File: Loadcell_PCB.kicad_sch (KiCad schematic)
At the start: 52 parts, among them J1 USB_C_Receptacle_USB2.0, J2 Load cell side, J3 Micro_SD_Card, Q1 S8550, SW1 RESET, U1 ATmega328P-M, U4 HX711, U5 74125, U6 LD1117S33TR_SOT223, U7 CH340C, Y1 16MHz

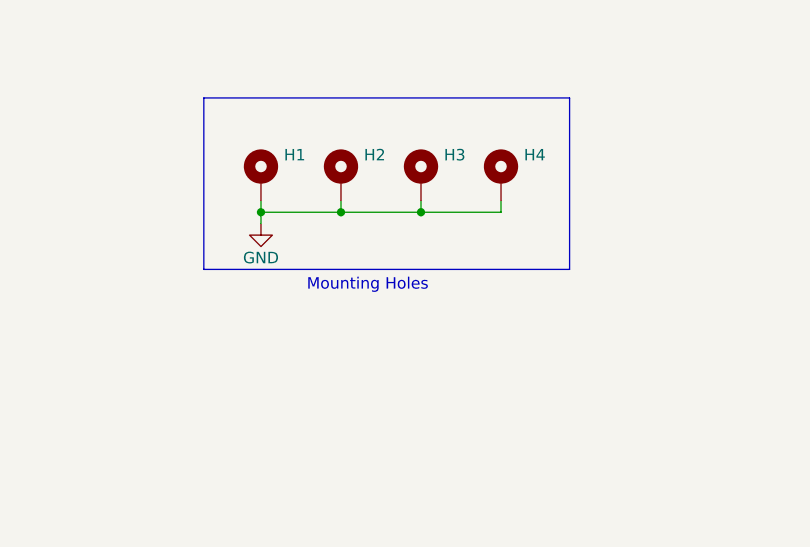
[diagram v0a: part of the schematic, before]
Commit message: some cleanup and add .gitignore
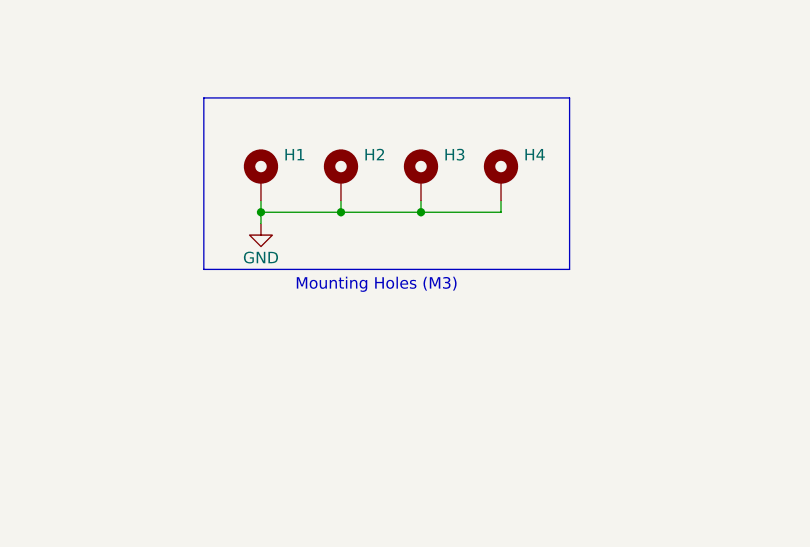
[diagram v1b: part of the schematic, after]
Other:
- note added: "Mounting Holes (M3)"
- note removed: "Mounting Holes"
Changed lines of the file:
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@@
     (effects (font (size 5 5)) (justify left bottom))
   )
-  (text "Mounting Holes\n" (at 203.2 242.57 0)
+  (text "Mounting Holes (M3)\n" (at 201.93 242.57 0)
     (effects (font (size 1.27 1.27)) (justify left bottom))
   )

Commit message: further cleanup for temp file
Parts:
- removed C4: 4u7F_16V, Capacitor_SMD:CP_Elec_4x3, symbol Device:C_Polarized
- removed D1: SS1P3L, Diode_SMD:D_Powermite_AK, symbol Device:D
- C6: renamed from C5; value 1uF -> 100nF
- renumbered C12 to C11, C13 to C12, C14 to C13, C15 to C14, C17 to C15, C9 to C2, C11 to C3, C3 to C4, C19 to C5, C6 to C7, C7 to C8, C18 to C9, D3 to D1, D6 to D3, D7 to D4, R17 to R1, R7 to R10, R9 to R11, R10 to R12, R12 to R13, R13 to R14, R14 to R15, R15 to R16, R16 to R2, R1 to R3, R2 to R4, R3 to R5, R4 to R6, R18 to R7, R19 to R8, R5 to R9, U7 to U2, U4 to U3, U5 to U4, U6 to U5
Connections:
- net VBUS is gone; now on net +5V: C2.1, C3.1, D1.1 (K)
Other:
- moved on the sheet: C4, C6

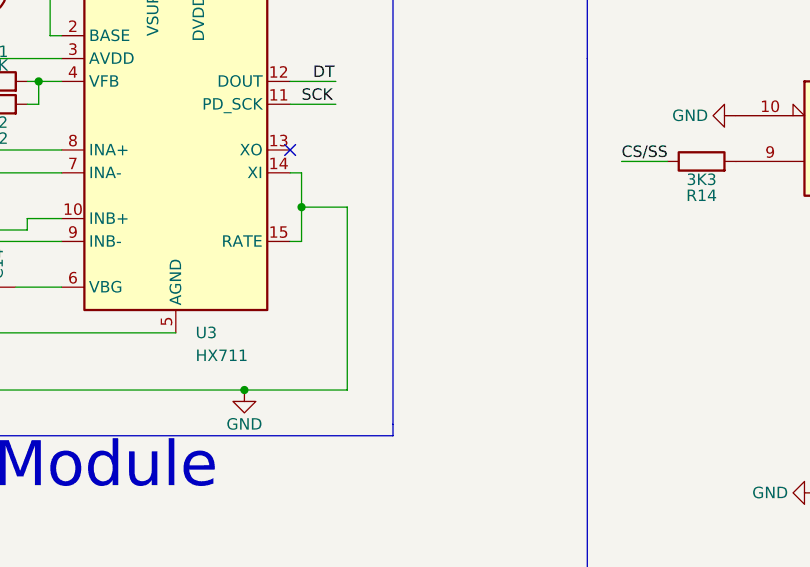
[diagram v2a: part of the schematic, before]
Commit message: Add pull-up resistor at rate pin on HX711 IC
Since HX711 can work in a higher frequency with rate pin pulled up, so I
add a optional structure that can select between two frequency by
soldering a ball at solder-jump bridge
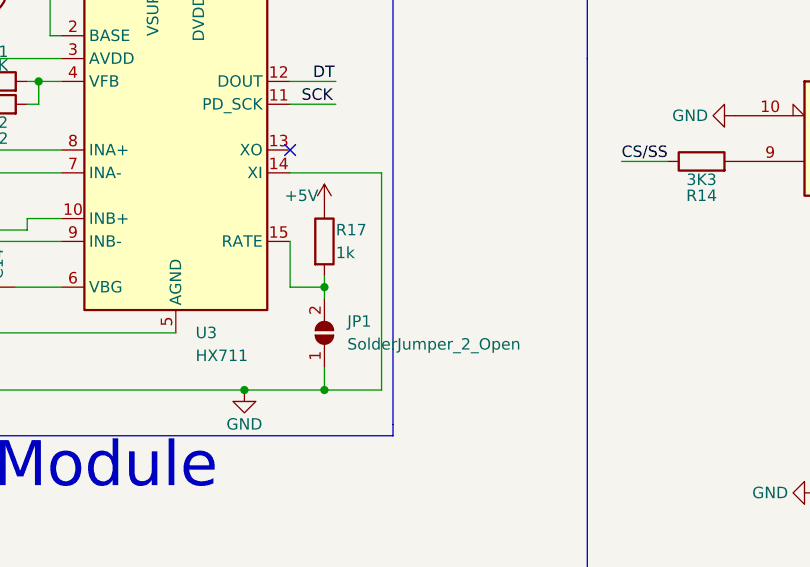
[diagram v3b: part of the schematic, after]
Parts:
- added JP1: SolderJumper_2_Open, Jumper:SolderJumper-2_P1.3mm_Open_RoundedPad1.0x1.5mm, symbol Jumper:SolderJumper_2_Open
- added R17: 1k, Resistor_SMD:R_0805_2012Metric_Pad1.20x1.40mm_HandSolder, symbol Device:R
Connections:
- net +5V: now also R17.1
- net GND: now also JP1.1 (A); no longer U3.15 (RATE)
- new net: JP1.2 (B), R17.2, U3.15 (RATE)
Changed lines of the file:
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@@
   (title_block
     (title "Loadcell_PCB")
-    (date "2024-02-08")
-    (rev "1.3")
+    (date "2024-03-06")
+    (rev "1.5")
     (company "NCKU_ISP")
     (comment 1 "https://hackmd.io/@ispncku/BywRPedI6")
@@
   (junction (at 198.12 233.68) (diameter 0) (color 0 0 0 0)
   )
-  (junction (at 260.35 152.4) (diameter 0) (color 0 0 0 0)
-  )
   (junction (at 69.85 154.94) (diameter 0) (color 0 0 0 0)
   )
@@
   (junction (at 243.84 120.65) (diameter 0) (color 0 0 0 0)
   )
+  (junction (at 262.89 161.29) (diameter 0) (color 0 0 0 0)
+  )
   (junction (at 218.44 144.78) (diameter 0) (color 0 0 0 0)
+  )
+  (junction (at 262.89 172.72) (diameter 0) (color 0 0 0 0)
   )
   (junction (at 54.61 167.64) (diameter 0) (color 0 0 0 0)
@@
     (stroke (width 0) (type default))
   )
+  (wire (pts (xy 259.08 156.21) (xy 259.08 161.29))
+    (stroke (width 0) (type default))
+  )
   (wire (pts (xy 198.12 156.21) (xy 198.12 148.59))
     (stroke (width 0) (type default))
@@
     (stroke (width 0) (type default))
   )
-  (wire (pts (xy 260.35 152.4) (xy 260.35 156.21))
+  (wire (pts (xy 259.08 161.29) (xy 262.89 161.29))
+    (stroke (width 0) (type default))
+  )
+  (wire (pts (xy 262.89 160.02) (xy 262.89 161.29))
     (stroke (width 0) (type default))
   )
@@
     (stroke (width 0) (type default))
   )
+  (wire (pts (xy 259.08 148.59) (xy 269.24 148.59))
+    (stroke (width 0) (type default))
+  )
   (wire (pts (xy 95.25 87.63) (xy 95.25 88.9))
     (stroke (width 0) (type default))
@@
     (stroke (width 0) (type default))
   )
-  (wire (pts (xy 265.43 172.72) (xy 265.43 152.4))
+  (wire (pts (xy 269.24 148.59) (xy 269.24 172.72))
     (stroke (width 0) (type default))
   )
@@
     (stroke (width 0) (type default))
   )
+  (wire (pts (xy 254 172.72) (xy 262.89 172.72))
+    (stroke (width 0) (type default))
+  )
+  (wire (pts (xy 262.89 161.29) (xy 262.89 162.56))
+    (stroke (width 0) (type default))
+  )
   (wire (pts (xy 53.34 167.64) (xy 54.61 167.64))
     (stroke (width 0) (type default))
@@
     (stroke (width 0) (type default))
   )
+  (wire (pts (xy 262.89 172.72) (xy 269.24 172.72))
+    (stroke (width 0) (type default))
+  )
   (wire (pts (xy 218.44 161.29) (xy 220.98 161.29))
     (stroke (width 0) (type default))
@@
     (stroke (width 0) (type default))
   )
-  (wire (pts (xy 265.43 152.4) (xy 260.35 152.4))
-    (stroke (width 0) (type default))
-  )
   (wire (pts (xy 146.05 160.02) (xy 151.13 160.02))
     (stroke (width 0) (type default))
   )
-  (wire (pts (xy 260.35 156.21) (xy 259.08 156.21))
-    (stroke (width 0) (type default))
-  )
   (wire (pts (xy 38.1 187.96) (xy 38.1 185.42))
     (stroke (width 0) (type default))
@@
     (stroke (width 0) (type default))
   )
-  (wire (pts (xy 254 172.72) (xy 265.43 172.72))
-    (stroke (width 0) (type default))
-  )
   (wire (pts (xy 93.98 35.56) (xy 93.98 38.1))
     (stroke (width 0) (type default))
@@
     (stroke (width 0) (type default))
   )
-  (wire (pts (xy 260.35 148.59) (xy 260.35 152.4))
-    (stroke (width 0) (type default))
-  )
   (wire (pts (xy 218.44 144.78) (xy 218.44 161.29))
     (stroke (width 0) (type default))
@@
     (stroke (width 0) (type default))
   )
-  (wire (pts (xy 259.08 148.59) (xy 260.35 148.59))
-    (stroke (width 0) (type default))
-  )
   (wire (pts (xy 53.34 152.4) (xy 57.15 152.4))
     (stroke (width 0) (type default))
@@
   )
   (wire (pts (xy 99.06 77.47) (xy 83.82 77.47))
+    (stroke (width 0) (type default))
+  )
+  (wire (pts (xy 262.89 170.18) (xy 262.89 172.72))
     (stroke (width 0) (type default))
   )
@@
     )
   )
+  (symbol (lib_id "Device:R") (at 262.89 156.21 0) (unit 1)
+    (in_bom yes) (on_board yes) (dnp no)
+    (property "Reference" "R17" (at 264.16 154.94 0)
+      (effects (font (size 1.27 1.27)) (justify left))
+    )
+    (property "Value" "1k" (at 264.16 157.48 0)
+      (effects (font (size 1.27 1.27)) (justify left))
+    )
+    (property "Footprint" "Resistor_SMD:R_0805_2012Metric_Pad1.20x1.40mm_HandSolder" (at 261.112 156.21 90)
+      (effects (font (size 1.27 1.27)) hide)
+    )
+    (property "Datasheet" "~" (at 262.89 156.21 0)
+      (effects (font (size 1.27 1.27)) hide)
+    )
+    (pin "1")
+    (pin "2")
+    (instances
+      (project "Loadcell_PCB"
+        (path "/59cf3c94-0731-4004-8b49-b268fb920fa8"
+          (reference "R17") (unit 1)
+        )
+      )
+    )
+  )
   (symbol (lib_id "power:+5V") (at 93.98 34.29 0) (unit 1)
     (in_bom yes) (on_board yes) (dnp no)
@@
     )
   )
+  (symbol (lib_id "Jumper:SolderJumper_2_Open") (at 262.89 166.37 90) (unit 1)
+    (in_bom yes) (on_board yes) (dnp no)
+    (property "Reference" "JP1" (at 265.43 165.1 90)
+      (effects (font (size 1.27 1.27)) (justify right))
+    )
+    (property "Value" "SolderJumper_2_Open" (at 265.43 167.64 90)
+      (effects (font (size 1.27 1.27)) (justify right))
+    )
+    (property "Footprint" "Jumper:SolderJumper-2_P1.3mm_Open_RoundedPad1.0x1.5mm" (at 262.89 166.37 0)
+      (effects (font (size 1.27 1.27)) hide)
+    )
+    (property "Datasheet" "~" (at 262.89 166.37 0)
+      (effects (font (size 1.27 1.27)) hide)
+    )
+    (pin "2")
+    (pin "1")
+    (instances
+      (project "Loadcell_PCB"
+        (path "/59cf3c94-0731-4004-8b49-b268fb920fa8"
+          (reference "JP1") (unit 1)
+        )
+      )
+    )
+  )
   (symbol (lib_id "Device:C") (at 123.19 184.15 0) (unit 1)
     (in_bom yes) (on_board yes) (dnp no)
@@
         )
       )
+    )
+  )
+  (symbol (lib_id "power:+5V") (at 262.89 152.4 0) (unit 1)
+    (in_bom yes) (on_board yes) (dnp no)
+    (property "Reference" "#PWR035" (at 262.89 156.21 0)
+      (effects (font (size 1.27 1.27)) hide)
+    )
+    (property "Value" "+5V" (at 260.35 151.13 0)
+      (effects (font (size 1.27 1.27)))
+    )
+    (property "Footprint" "" (at 262.89 152.4 0)
+      (effects (font (size 1.27 1.27)) hide)
+    )
+    (property "Datasheet" "" (at 262.89 152.4 0)
+      (effects (font (size 1.27 1.27)) hide)
+    )
+    (pin "1")
+    (instances
+      (project "Loadcell_PCB"
+        (path "/59cf3c94-0731-4004-8b49-b268fb920fa8"
+          (reference "#PWR035") (unit 1)
+        )
+      )

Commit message: Add an extra UART channel for GPS
In order to recieve GPS and serail print signals at the same time,
we need more than only one UART channel which is used as the serial
print channel by default, So now the second UART channel is added
and the implementation will be done by software.
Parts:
- added J4: GPS, Connector_PinHeader_2.54mm:PinHeader_1x02_P2.54mm_Horizontal, symbol Connector_Generic:Conn_01x02
- JP1: value SolderJumper_2_Open -> pull up
- R3, R4: value 1K -> 330
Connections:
- net RX: now also U1.31 (PD1); no longer R4.2
- net TX: now also U1.30 (PD0); no longer R3.2
- net at U1.25 (PC2): now also R3.1
- net at U1.26 (PC3): now also R4.1
- new net RX2: J4.1 (Pin_1), R4.2
- new net TX2: J4.2 (Pin_2), R3.2
- no-connect marks 25 -> 23
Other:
- moved on the sheet: R5, SW1

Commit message: Update unsaved record to the current commit
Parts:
- renumbered J4 to J2, J2 to J3, J3 to J4, R17 to R13, R13 to R14, R14 to R15, R15 to R16, R16 to R17, R6 to R5, R5 to R6
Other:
- moved on the sheet: C1, C10, C11, C12, C13, C14, C15, C2, C3, C4, C5, C6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

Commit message: Prepare for next revision - PT initial edit
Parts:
- added J5: PT, Connector_PinHeader_2.54mm:PinHeader_1x02_P2.54mm_Horizontal, symbol Connector_Generic:Conn_01x02
- added J6: Barrel_Jack_Switch, symbol Connector:Barrel_Jack_Switch
- added R18: 250, Resistor_SMD:R_0805_2012Metric_Pad1.20x1.40mm_HandSolder, symbol Device:R
- J4: footprint Connector_Card:microSD_HC_Hirose_DM3BT-DSF-PEJS -> Connector_Card:microSD_HC_Molex_104031-0811
- U1: footprint Package_DFN_QFN:QFN-32-1EP_5x5mm_P0.5mm_EP3.1x3.1mm -> Package_QFP:TQFP-48-1EP_7x7mm_P0.5mm_EP5x5mm_ThermalVias
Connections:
- net GND: now also J6.1, J6.3, R18.2
- net PT_OUT: now reaches U1.23 (PC0)
- net PT_OUT: now also R18.1
- no-connect marks 23 -> 22
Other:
- moved on the sheet: C1, C2, C3, C4, C6, C7, C8, D2, J2, R3, R4, R5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

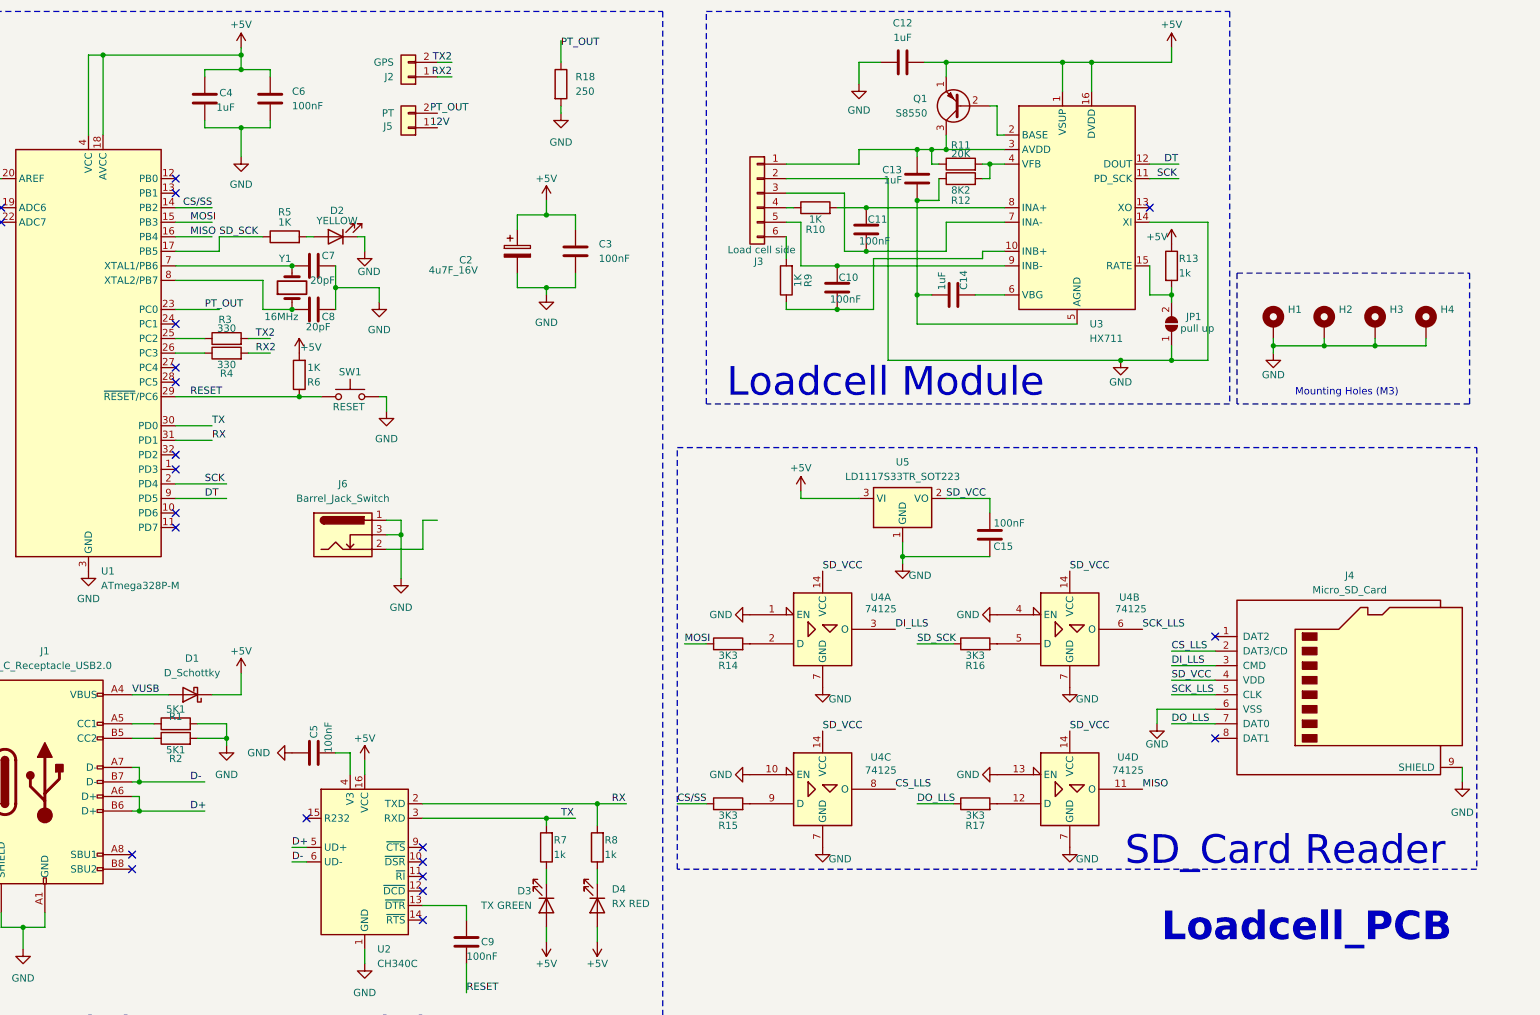
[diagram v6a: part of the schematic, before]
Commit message: Add new symbol and footprint for DC2DC converter
In order to power PT which requires 8V ~ 12V power supply, an 5V_12V
DC2DC converter in added into the schematic. Since the converter is
custom manufactured by an independent company, the correspond data
is not included in the Kicad library. So I have to draw it by my self.

Now, both symbol and footprint are finished, the next step is to
redraw the whole PCB layout and make it even more compact.
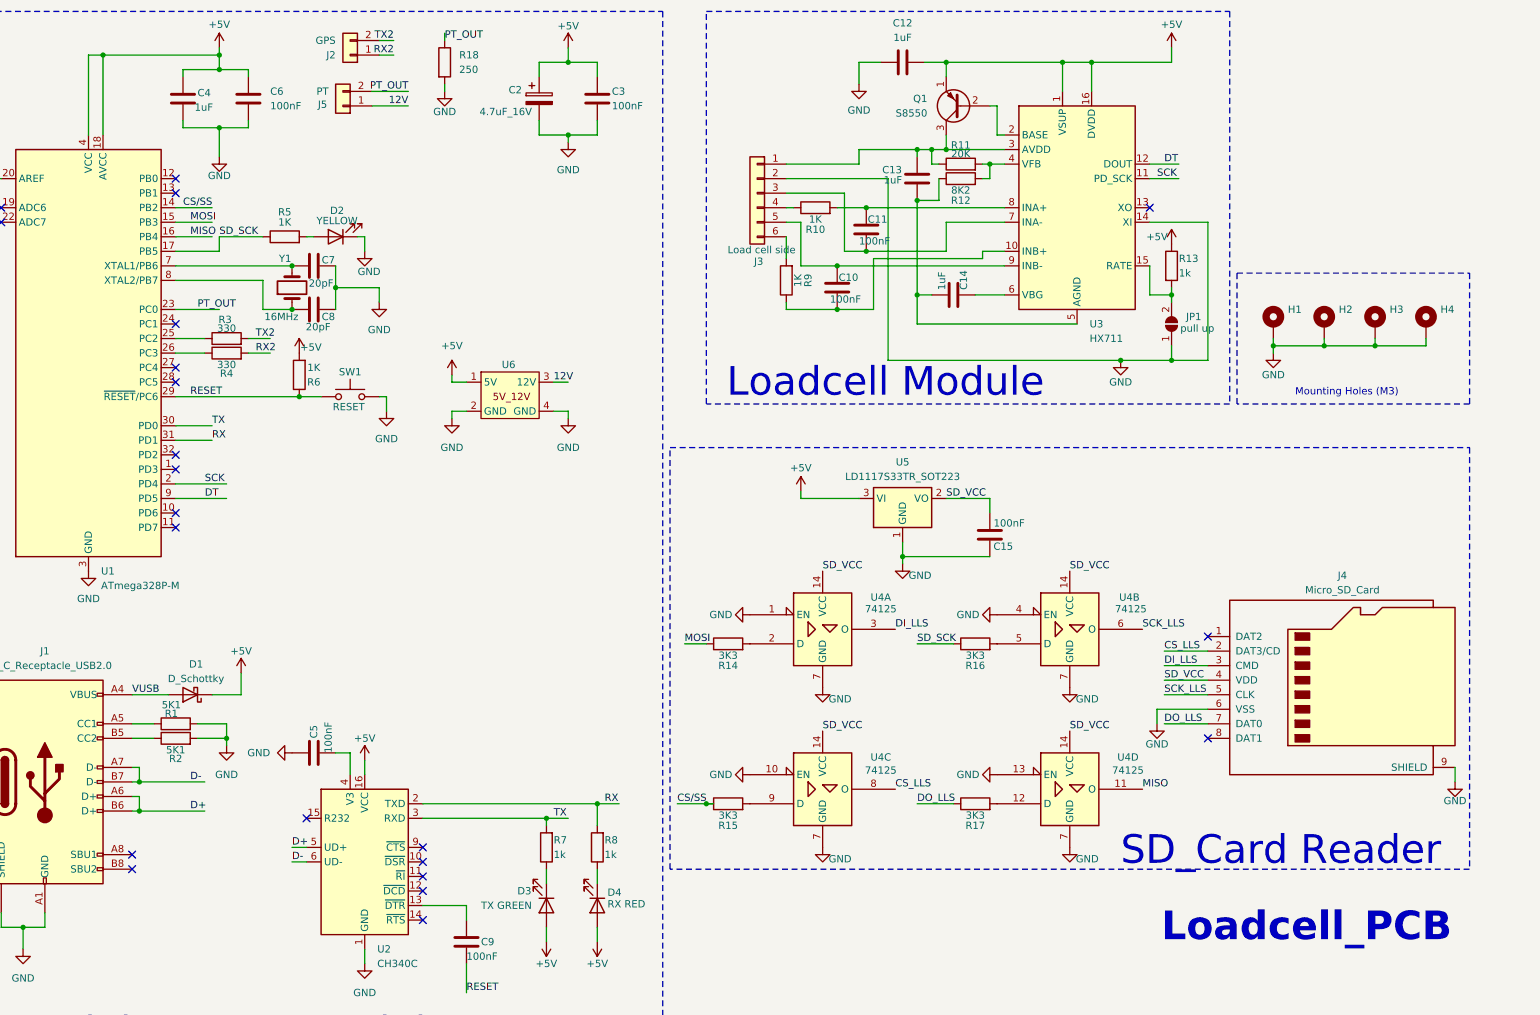
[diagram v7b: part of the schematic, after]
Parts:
- removed J6: Barrel_Jack_Switch, symbol Connector:Barrel_Jack_Switch
- added U6: ~, Custom_footprints:DC2DC, symbol Custom_symbols:DC2DC
- C2: value 4u7F_16V -> 4.7uF_16V
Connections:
- net +5V: now also U6.1 (5V)
- net 12V: now also J5.1 (Pin_1), U6.3 (12V)
- net GND: now also U6.2 (GND), U6.4 (GND)
- net PT_OUT: now also J5.2 (Pin_2)
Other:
- moved on the sheet: C2, C3, C4, C6, J2, J4, J5, R18
